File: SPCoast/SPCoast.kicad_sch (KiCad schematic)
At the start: 0 parts

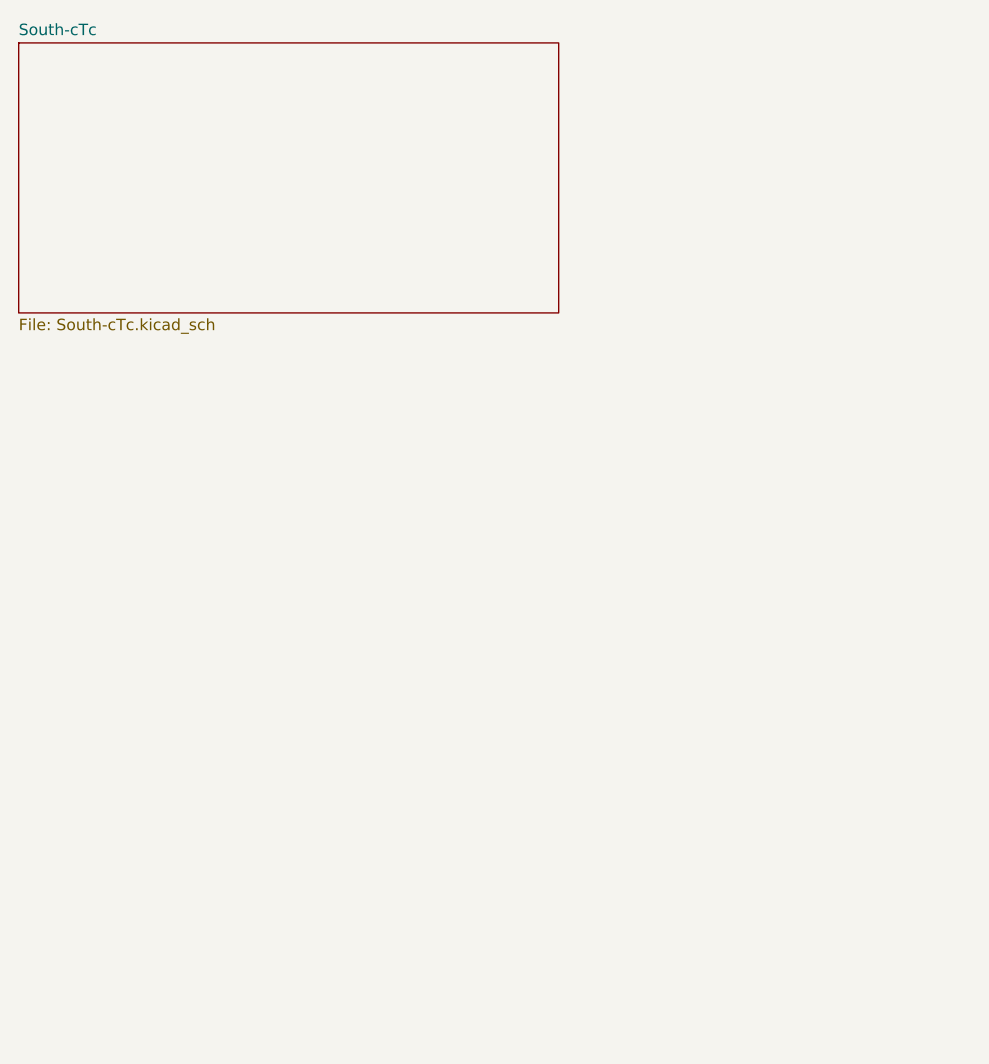
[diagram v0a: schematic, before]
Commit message: chore(kicad): owner edits (2026-10-23): Railroad symbol added to Railroad-Office and placed on the root sheet
Baseline before the scripted move of Railroad and Era off the OfficeUnit and the macro Topic.

Co-Authored-By: Claude Fable 5.1 <noreply@anthropic.com>
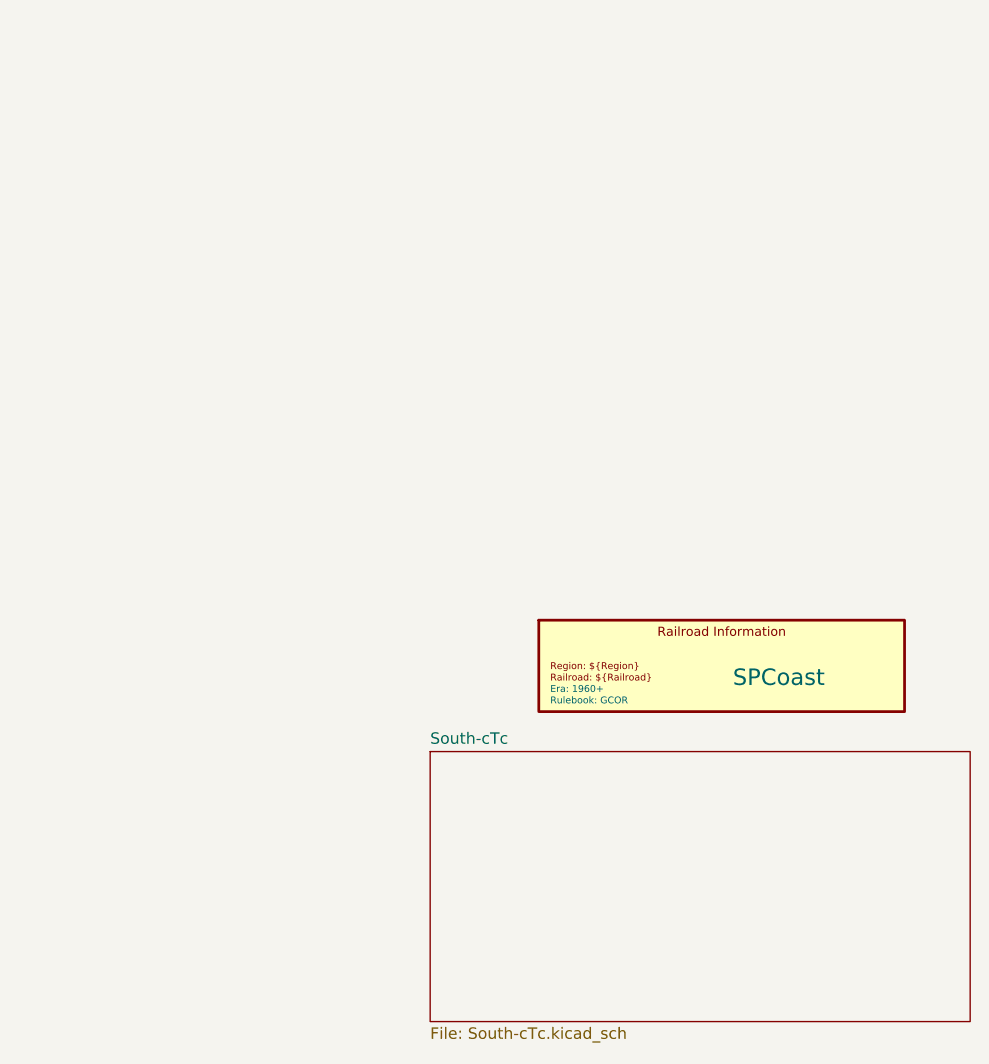
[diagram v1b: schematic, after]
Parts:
- added RAILROAD1: SPCoast, symbol Railroad-Office:Railroad
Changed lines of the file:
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@@
 		(comment 9 "active")
 	)
+	(symbol
+		(lib_id "Railroad-Office:Railroad")
+		(at 118.11 109.22 0)
+		(unit 1)
+		(body_style 1)
+		(exclude_from_sim no)
+		(in_bom yes)
+		(on_board yes)
+		(in_pos_files yes)
+		(dnp no)
+		(fields_autoplaced yes)
+		(property "Reference" "RAILROAD1"
+			(at 102.362 100.584 0)
+			(hide yes)
+			(show_name no)
+			(do_not_autoplace yes)
+			(effects
+				(font
+					(size 1.27 1.27)
+				)
+			)
+		)
+		(property "Value" "SPCoast"
+			(at 121.158 101.6 0)
+			(hide yes)
+			(show_name no)
+			(do_not_autoplace yes)
+			(effects
+				(font
+					(size 1.27 1.27)
+				)
+			)
+		)
+		(property "Footprint" ""
+			(at 118.11 109.22 0)
+			(hide yes)
+			(show_name no)
+			(do_not_autoplace no)
+			(effects
+				(font
+					(size 1.27 1.27)
+				)
+			)
+		)
+		(property "Datasheet" ""
+			(at 118.11 109.22 0)
+			(hide yes)
+			(show_name no)
+			(do_not_autoplace no)
+			(effects
+				(font
+					(size 1.27 1.27)
+				)
+			)
+		)
+		(property "Description" "Attributes for the railroad itself"
+			(at 127.635 116.205 0)
+			(hide yes)
+			(show_name no)
+			(do_not_autoplace no)
+			(effects
+				(font
+					(size 1.27 1.27)
+				)
+			)
+		)
+		(property "Role" "STRUCTURE"
+			(at 102.108 101.981 0)
+			(hide yes)
+			(show_name no)
+			(do_not_autoplace yes)
+			(effects
+				(font
+					(size 1.016 1.016)
+				)
+			)
+		)
+		(property "Kind" "RAILROAD"
+			(at 100.457 103.124 0)
+			(hide yes)
+			(show_name no)
+			(do_not_autoplace yes)
+			(effects
+				(font
+					(size 0.762 0.762)
+				)
+			)
+		)
+		(property "Era" "1960+"
+			(at 99.06 111.76 0)
+			(show_name yes)
+			(do_not_autoplace yes)
+			(effects
+				(font
+					(size 0.762 0.762)
+				)
+				(justify left)
+			)
+		)
+		(property "Railroad" "Southern Pacific"
+			(at 126.238 118.491 0)
+			(hide yes)
+			(show_name no)
+			(do_not_autoplace yes)
+			(effects
+				(font
+					(size 0.762 0.762)
+				)
+				(justify left)
+			)
+		)
+		(property "Region" "Coast Line"
+			(at 129.286 119.761 0)
+			(hide yes)
+			(show_name no)
+			(do_not_autoplace yes)
+			(effects
+				(font
+					(size 0.762 0.762)
+				)
+			)
+		)
+		(property "Rulebook" "GCOR"
+			(at 99.06 113.03 0)
+			(show_name yes)
+			(do_not_autoplace yes)
+			(effects
+				(font
+					(size 0.762 0.762)
+				)
+				(justify left)
+			)
+		)
+		(property "Name" "${Value}"
+			(at 124.46 110.49 0)
+			(show_name no)
+			(do_not_autoplace yes)
+			(effects
+				(font
+					(size 1.8288 1.8288)
+				)
+			)
+		)
+		(instances
+			(project "SPCoast"
+				(path "/528348b2-add8-5367-a5f7-439c76f0ca33"
+					(reference "RAILROAD1")
+					(unit 1)
+				)
+			)
+		)
+	)
 	(sheet
-		(at 40 40)
+		(at 85.72 118.74)
 		(size 60 30)
 		(exclude_from_sim no)
@@
 		)
 		(property "Sheetname" "South-cTc"
-			(at 40 39.2884 0)
+			(at 85.72 118.0284 0)
 			(show_name no)
 			(do_not_autoplace no)
@@
 		)
 		(property "Sheetfile" "South-cTc.kicad_sch"
-			(at 40 70.5846 0)
+			(at 85.72 149.3246 0)
 			(show_name no)
 			(do_not_autoplace no)
